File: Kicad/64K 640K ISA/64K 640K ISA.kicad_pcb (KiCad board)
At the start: 2 copper layers, 104 x 73.9 mm, 17 parts, among them J9 Bus_ISA_8bit, U1 64K, U2 64K, U3 AS6C1008, U4 AS6C4008, U5 74LS139, U6 74LS138

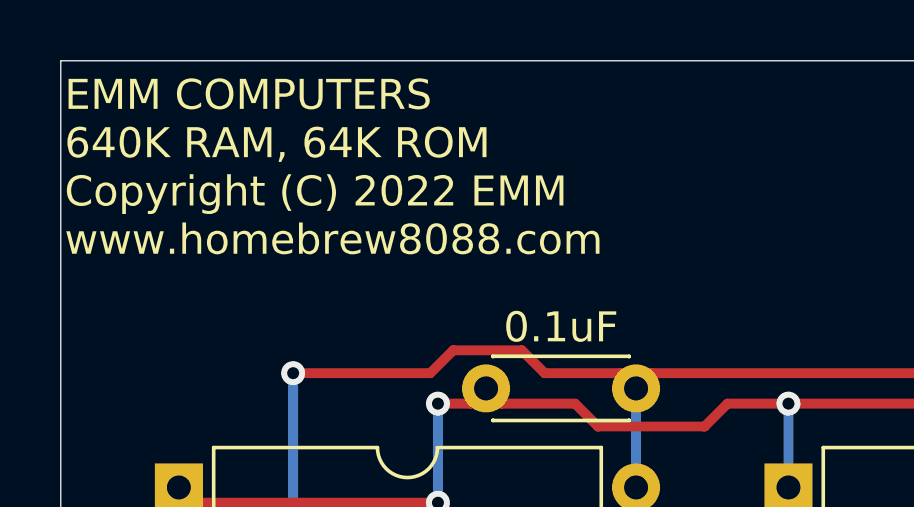
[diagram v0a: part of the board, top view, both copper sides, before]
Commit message: updated DMA
Added DMA controller to main board.
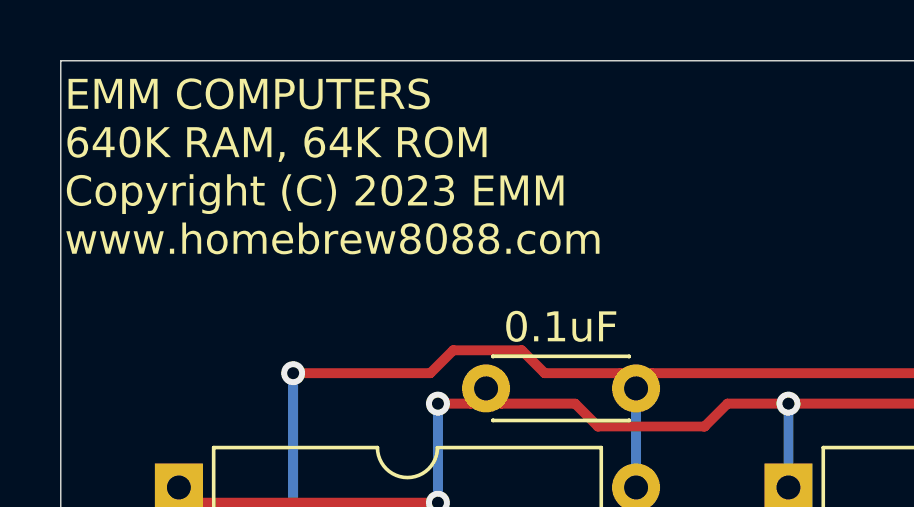
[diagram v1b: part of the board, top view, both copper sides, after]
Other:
- board text added: "EMM COMPUTERS 640K RAM, 64K ROM Copyright (C) 2023 EMM www.homebrew8088.com"
- board text removed: "EMM COMPUTERS 640K RAM, 64K ROM Copyright (C) 2022 EMM www.homebrew8088.com"
